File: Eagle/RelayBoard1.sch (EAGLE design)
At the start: 12 parts, among them IC1 ULN2003AN, K1 4052, K2 4052, K3 4051, X1 MKDSN1,5/6-5,08, X2 MKDSN1,5/6-5,08, X3 CON1, X4 MKDSN1,5/3-5,08, X7 CON2

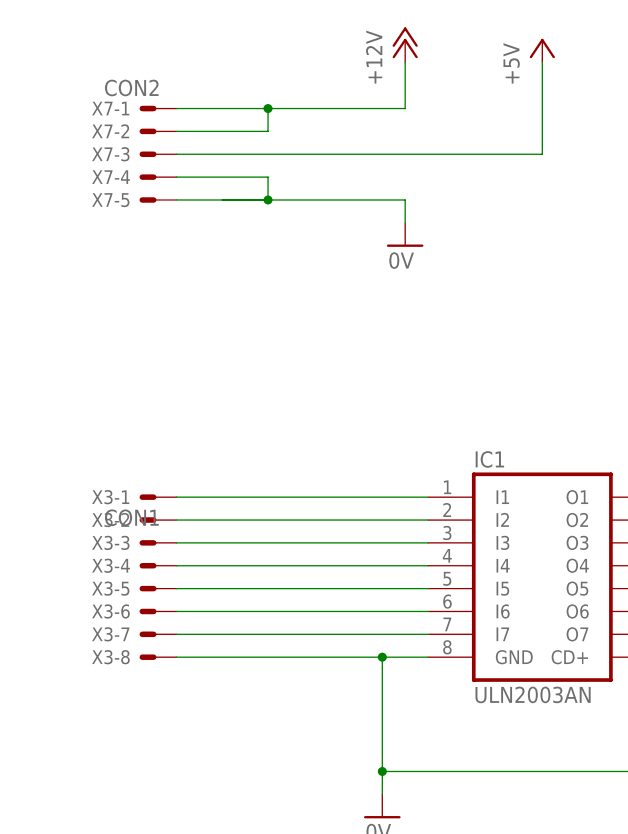
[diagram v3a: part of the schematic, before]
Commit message: - corrections for RelayBoard1:   - using right connectors from library con-molex   - single sided routing - corrections for ButtonBoard:   - using right connector from library con-molex   - using right switches from library switch-misc (SRK/SRKL) - component placement & board layout for ButtonBoard done - CPUBoard:   - some components moved around the board   - re-routing (partially)
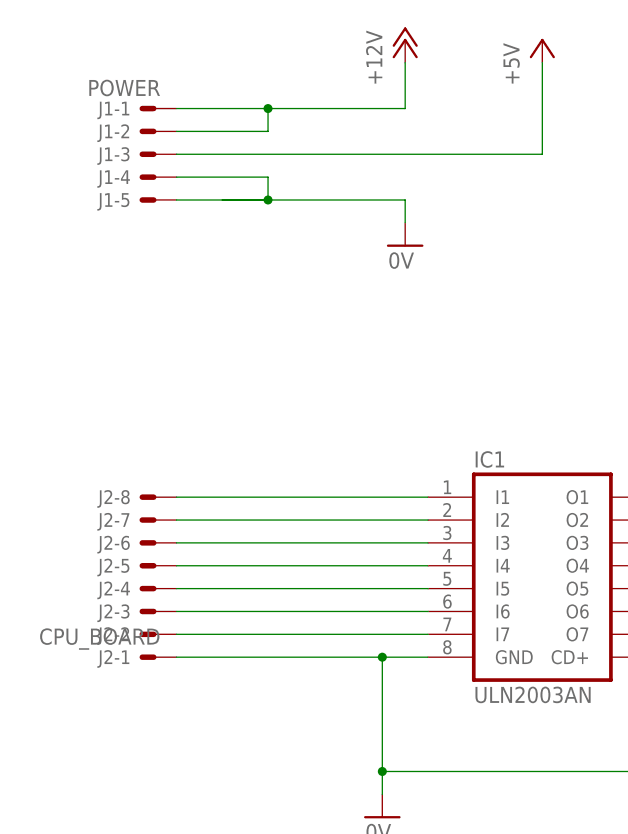
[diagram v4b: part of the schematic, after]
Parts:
- removed X3: CON1, con-molex:KK-156-8
- removed X7: CON2, con-molex:KK-156-5
- added J1: POWER, con-molex:22-27-2051-05
- added J2: CPU_BOARD, con-molex:22-27-2081-08
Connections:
- removed net N$24: IC1.I7, X3-7.S
- new net N$5: IC1.I1, J2-8.S
- net +12V: now also J1-1.S, J1-2.S; no longer X7-1.S, X7-2.S
- net +5V: now also J1-3.S; no longer X7-3.S
- net 0V: now also J1-4.S, J1-5.S, J2-1.S; no longer X3-8.S, X7-4.S, X7-5.S
- net N$18: now also IC1.I2, J2-7.S; no longer IC1.I1, X3-1.S
- net N$19: now also IC1.I3, J2-6.S; no longer IC1.I2, X3-2.S
- net N$20: now also IC1.I4, J2-5.S; no longer IC1.I3, X3-3.S
- net N$21: now also IC1.I5, J2-4.S; no longer IC1.I4, X3-4.S
- net N$22: now also IC1.I6, J2-3.S; no longer IC1.I5, X3-5.S
- net N$23: now also IC1.I7, J2-2.S; no longer IC1.I6, X3-6.S
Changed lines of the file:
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@@
 <part name="P+7" library="supply1" deviceset="+12V" device=""/>
 <part name="P+3" library="supply1" deviceset="+12V" device=""/>
-<part name="X7" library="con-molex" deviceset="KK-156-5" device="" value="CON2"/>
 <part name="X8" library="con-molex" deviceset="KK-156-3" device=""/>
 <part name="X9" library="con-molex" deviceset="KK-156-3" device=""/>
@@
 <attribute name="OC_NEWARK" value="70R0299"/>
 </part>
-<part name="X3" library="con-molex" deviceset="KK-156-8" device="" value="CON1"/>
+<part name="J1" library="con-molex" deviceset="22-?-05" device="27-2051" value="POWER"/>
+<part name="J2" library="con-molex" deviceset="22-?-08" device="27-2081" value="CPU_BOARD"/>
 </parts>
 <sheets>
@@
 <instance part="P+7" gate="1" x="182.88" y="91.44"/>
 <instance part="P+3" gate="1" x="78.74" y="129.54"/>
-<instance part="X7" gate="-1" x="15.24" y="162.56" rot="MR0"/>
-<instance part="X7" gate="-2" x="15.24" y="160.02" rot="MR0"/>
-<instance part="X7" gate="-3" x="15.24" y="157.48" rot="MR0"/>
-<instance part="X7" gate="-4" x="15.24" y="154.94" rot="MR0"/>
-<instance part="X7" gate="-5" x="15.24" y="152.4" rot="MR0"/>
 <instance part="X8" gate="-1" x="96.52" y="58.42" rot="R270"/>
 <instance part="X8" gate="-2" x="99.06" y="58.42" rot="R270"/>
@@
 <instance part="X4" gate="-2" x="246.38" y="165.1"/>
 <instance part="X4" gate="-3" x="246.38" y="160.02"/>
-<instance part="X3" gate="-1" x="15.24" y="119.38" rot="R180"/>
-<instance part="X3" gate="-2" x="15.24" y="116.84" rot="R180"/>
-<instance part="X3" gate="-3" x="15.24" y="114.3" rot="R180"/>
-<instance part="X3" gate="-4" x="15.24" y="111.76" rot="R180"/>
-<instance part="X3" gate="-5" x="15.24" y="109.22" rot="R180"/>
-<instance part="X3" gate="-6" x="15.24" y="106.68" rot="R180"/>
-<instance part="X3" gate="-7" x="15.24" y="104.14" rot="R180"/>
-<instance part="X3" gate="-8" x="15.24" y="101.6" rot="R180"/>
+<instance part="J1" gate="-1" x="15.24" y="162.56" rot="MR0"/>
+<instance part="J1" gate="-2" x="15.24" y="160.02" rot="MR0"/>
+<instance part="J1" gate="-3" x="15.24" y="157.48" rot="MR0"/>
+<instance part="J1" gate="-4" x="15.24" y="154.94" rot="MR0"/>
+<instance part="J1" gate="-5" x="15.24" y="152.4" rot="MR0"/>
+<instance part="J2" gate="-1" x="15.24" y="101.6" rot="MR0"/>
+<instance part="J2" gate="-2" x="15.24" y="104.14" rot="MR0"/>
+<instance part="J2" gate="-3" x="15.24" y="106.68" rot="MR0"/>
+<instance part="J2" gate="-4" x="15.24" y="109.22" rot="MR0"/>
+<instance part="J2" gate="-5" x="15.24" y="111.76" rot="MR0"/>
+<instance part="J2" gate="-6" x="15.24" y="114.3" rot="MR0"/>
+<instance part="J2" gate="-7" x="15.24" y="116.84" rot="MR0"/>
+<instance part="J2" gate="-8" x="15.24" y="119.38" rot="MR0"/>
 </instances>
 <busses>
@@
 <pinref part="P+2" gate="1" pin="+5V"/>
 <wire x1="58.42" y1="157.48" x2="58.42" y2="167.64" width="0.1524" layer="91"/>
-<pinref part="X7" gate="-3" pin="S"/>
+<pinref part="J1" gate="-3" pin="S"/>
 </segment>
 </net>
@@
 <wire x1="43.18" y1="152.4" x2="43.18" y2="149.86" width="0.1524" layer="91"/>
 <junction x="27.94" y="152.4"/>
-<pinref part="X7" gate="-5" pin="S"/>
 <wire x1="17.78" y1="152.4" x2="27.94" y2="152.4" width="0.1524" layer="91"/>
-<pinref part="X7" gate="-4" pin="S"/>
 <wire x1="27.94" y1="154.94" x2="17.78" y2="154.94" width="0.1524" layer="91"/>
+<pinref part="J1" gate="-4" pin="S"/>
+<pinref part="J1" gate="-5" pin="S"/>
 </segment>
 <segment>
@@
 <wire x1="45.72" y1="101.6" x2="40.64" y2="101.6" width="0.1524" layer="91"/>
 <wire x1="40.64" y1="88.9" x2="40.64" y2="101.6" width="0.1524" layer="91"/>
-<wire x1="40.64" y1="101.6" x2="17.78" y2="101.6" width="0.1524" layer="91"/>
-<junction x="40.64" y="101.6"/>
 <pinref part="GND2" gate="1" pin="0V"/>
 <wire x1="40.64" y1="86.36" x2="40.64" y2="88.9" width="0.1524" layer="91"/>
 <junction x="40.64" y="88.9"/>
-<pinref part="X3" gate="-8" pin="S"/>
-</segment>
-</net>
-<net name="N$18" class="0">
-<segment>
-<pinref part="IC1" gate="A" pin="I1"/>
-<wire x1="45.72" y1="119.38" x2="17.78" y2="119.38" width="0.1524" layer="91"/>
-<pinref part="X3" gate="-1" pin="S"/>
-</segment>
-</net>
-<net name="N$19" class="0">
-<segment>
-<pinref part="IC1" gate="A" pin="I2"/>
-<wire x1="45.72" y1="116.84" x2="17.78" y2="116.84" width="0.1524" layer="91"/>
-<pinref part="X3" gate="-2" pin="S"/>
-</segment>
-</net>
-<net name="N$20" class="0">
-<segment>
-<pinref part="IC1" gate="A" pin="I3"/>
-<wire x1="45.72" y1="114.3" x2="17.78" y2="114.3" width="0.1524" layer="91"/>
-<pinref part="X3" gate="-3" pin="S"/>
-</segment>
-</net>
-<net name="N$21" class="0">
-<segment>
-<pinref part="IC1" gate="A" pin="I4"/>
-<wire x1="45.72" y1="111.76" x2="17.78" y2="111.76" width="0.1524" layer="91"/>
-<pinref part="X3" gate="-4" pin="S"/>
-</segment>
-</net>
-<net name="N$22" class="0">
-<segment>
-<pinref part="IC1" gate="A" pin="I5"/>
-<wire x1="45.72" y1="109.22" x2="17.78" y2="109.22" width="0.1524" layer="91"/>
-<pinref part="X3" gate="-5" pin="S"/>
-</segment>
-</net>
-<net name="N$23" class="0">
-<segment>
-<pinref part="IC1" gate="A" pin="I6"/>
-<wire x1="45.72" y1="106.68" x2="17.78" y2="106.68" width="0.1524" layer="91"/>
-<pinref part="X3" gate="-6" pin="S"/>
-</segment>
-</net>
-<net name="N$24" class="0">
-<segment>
-<pinref part="IC1" gate="A" pin="I7"/>
-<wire x1="45.72" y1="104.14" x2="17.78" y2="104.14" width="0.1524" layer="91"/>
-<pinref part="X3" gate="-7" pin="S"/>
+<pinref part="J2" gate="-1" pin="S"/>
+<wire x1="40.64" y1="101.6" x2="17.78" y2="101.6" width="0.1524" layer="91"/>
+<junction x="40.64" y="101.6"/>
 </segment>
 </net>
@@
 <wire x1="27.94" y1="162.56" x2="27.94" y2="160.02" width="0.1524" layer="91"/>
 <junction x="27.94" y="162.56"/>
-<pinref part="X7" gate="-2" pin="S"/>
 <wire x1="27.94" y1="160.02" x2="17.78" y2="160.02" width="0.1524" layer="91"/>
-<pinref part="X7" gate="-1" pin="S"/>
 <wire x1="27.94" y1="162.56" x2="17.78" y2="162.56" width="0.1524" layer="91"/>
+<pinref part="J1" gate="-1" pin="S"/>
+<pinref part="J1" gate="-2" pin="S"/>
 </segment>
 <segment>
@@
 </segment>
 </net>
+<net name="N$5" class="0">
+<segment>
+<pinref part="J2" gate="-8" pin="S"/>
+<pinref part="IC1" gate="A" pin="I1"/>
+<wire x1="17.78" y1="119.38" x2="45.72" y2="119.38" width="0.1524" layer="91"/>
+</segment>
+</net>
+<net name="N$18" class="0">
+<segment>
+<pinref part="IC1" gate="A" pin="I2"/>
+<pinref part="J2" gate="-7" pin="S"/>
+<wire x1="45.72" y1="116.84" x2="17.78" y2="116.84" width="0.1524" layer="91"/>
+</segment>
+</net>
+<net name="N$19" class="0">
+<segment>
+<pinref part="J2" gate="-6" pin="S"/>
+<pinref part="IC1" gate="A" pin="I3"/>
+<wire x1="17.78" y1="114.3" x2="45.72" y2="114.3" width="0.1524" layer="91"/>
+</segment>
+</net>
+<net name="N$20" class="0">
+<segment>
+<pinref part="IC1" gate="A" pin="I4"/>
+<pinref part="J2" gate="-5" pin="S"/>
+<wire x1="45.72" y1="111.76" x2="17.78" y2="111.76" width="0.1524" layer="91"/>
+</segment>
+</net>
+<net name="N$21" class="0">
+<segment>
+<pinref part="J2" gate="-4" pin="S"/>
+<pinref part="IC1" gate="A" pin="I5"/>
+<wire x1="17.78" y1="109.22" x2="45.72" y2="109.22" width="0.1524" layer="91"/>
+</segment>
+</net>
+<net name="N$22" class="0">
+<segment>
+<pinref part="IC1" gate="A" pin="I6"/>
+<pinref part="J2" gate="-3" pin="S"/>
+<wire x1="45.72" y1="106.68" x2="17.78" y2="106.68" width="0.1524" layer="91"/>
+</segment>
+</net>
+<net name="N$23" class="0">
+<segment>
+<pinref part="J2" gate="-2" pin="S"/>
+<pinref part="IC1" gate="A" pin="I7"/>
+<wire x1="17.78" y1="104.14" x2="45.72" y2="104.14" width="0.1524" layer="91"/>
+</segment>
+</net>
